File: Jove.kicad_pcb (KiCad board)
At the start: 2 copper layers, 65 x 100 mm, 153 parts, among them J1 PJ301B, J2 PJ301B, J3 PJ301B, J4 PJ301B, J5 PJ301B, J6 PJ301B, P1 CONN_02X05, Q1 BCM857BS, Q2 BCM857BS, Q3 J112, Q4 J112, Q5 J112, Q6 J112, SW1 KS-01Q, U1 TL072-, U10 CD4027, U11 CD40106, U12 TS321, U13 TS321, U2 TL072-, U3 TL072-, U4 TL072-, U5 LM13700, U6 LM13700, U7 LM13700, U8 DG409, U9 CD4052

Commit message: commit before making panel branch
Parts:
- added REF**: fiducial-1mm, MyModules:fiducial-1mm, B.Cu at (15.0, 15.0)
- added REF**: fiducial-1mm, MyModules:fiducial-1mm, B.Cu at (74.5, 109.5)
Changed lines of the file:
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@@
     (thickness 1.6)
     (drawings 45)
-    (tracks 1170)
+    (tracks 1171)
     (zones 0)
-    (modules 153)
+    (modules 155)
     (nets 114)
   )
@@
     (pad_to_mask_clearance 0)
     (aux_axis_origin 0 0)
-    (visible_elements 7FFFB7FF)
+    (visible_elements 7FFFF77F)
     (pcbplotparams
       (layerselection 0x010f0_80000001)
@@
     (add_net -12V)
   )
+  (module MyModules:SM0603-R-JRL (layer B.Cu)
+    (at 17.8 21.75 270)
+    (attr smd)
+    (fp_text reference R76 (at 2 -0.1 360) (layer B.SilkS)
+      (effects (font (size 0.6096 0.6096) (thickness 0.1524)) (justify mirror))
+    )
+    (fp_text value 100K (at 0 0 270) (layer B.SilkS) hide
+      (effects (font (size 0.508 0.4572) (thickness 0.1143)) (justify mirror))
+    )
+    (fp_line (start -1.4 0.8) (end -0.5 0.8) (layer B.SilkS) (width 0.2))
+    (fp_line (start 1.4 -0.8) (end 1.4 0.8) (layer B.SilkS) (width 0.2))
+    (fp_line (start -1.4 0.8) (end -1.4 -0.8) (layer B.SilkS) (width 0.2))
+    (fp_line (start -1.4 -0.8) (end -0.5 -0.8) (layer B.SilkS) (width 0.2))
+    (fp_line (start 0.5 0.8) (end 1.4 0.8) (layer B.SilkS) (width 0.2))
+    (fp_line (start 0.5 -0.8) (end 1.4 -0.8) (layer B.SilkS) (width 0.2))
+    (pad 1 smd rect (at -0.8509 0 270) (size 0.8128 1.143) (layers B.Cu B.Paste B.Mask)
+      (net 85 "Net-(R76-Pad1)"))
+    (pad 2 smd rect (at 0.8509 0 270) (size 0.8128 1.143) (layers B.Cu B.Paste B.Mask)
+      (net 32 "Net-(J2-Pad3)"))
+    (model Resistors_SMD.3dshapes/R_0603.wrl
+      (at (xyz 0 0 0.001))
+      (scale (xyz 1 1 1))
+      (rotate (xyz 0 0 0))
+    )
+  )
   (module "SMD TRAN:sot323-6" (layer B.Cu)
     (at 37.75 26 270)
@@
   )
   (module MyModules:SM0603-R-JRL (layer B.Cu)
-    (at 17.8 21.75 270)
-    (attr smd)
-    (fp_text reference R76 (at 2 -0.1 360) (layer B.SilkS)
-      (effects (font (size 0.6096 0.6096) (thickness 0.1524)) (justify mirror))
-    )
-    (fp_text value 100K (at 0 0 270) (layer B.SilkS) hide
-      (effects (font (size 0.508 0.4572) (thickness 0.1143)) (justify mirror))
-    )
-    (fp_line (start -1.4 0.8) (end -0.5 0.8) (layer B.SilkS) (width 0.2))
-    (fp_line (start 1.4 -0.8) (end 1.4 0.8) (layer B.SilkS) (width 0.2))
-    (fp_line (start -1.4 0.8) (end -1.4 -0.8) (layer B.SilkS) (width 0.2))
-    (fp_line (start -1.4 -0.8) (end -0.5 -0.8) (layer B.SilkS) (width 0.2))
-    (fp_line (start 0.5 0.8) (end 1.4 0.8) (layer B.SilkS) (width 0.2))
-    (fp_line (start 0.5 -0.8) (end 1.4 -0.8) (layer B.SilkS) (width 0.2))
-    (pad 1 smd rect (at -0.8509 0 270) (size 0.8128 1.143) (layers B.Cu B.Paste B.Mask)
-      (net 85 "Net-(R76-Pad1)"))
-    (pad 2 smd rect (at 0.8509 0 270) (size 0.8128 1.143) (layers B.Cu B.Paste B.Mask)
-      (net 32 "Net-(J2-Pad3)"))
-    (model Resistors_SMD.3dshapes/R_0603.wrl
-      (at (xyz 0 0 0.001))
-      (scale (xyz 1 1 1))
-      (rotate (xyz 0 0 0))
-    )
-  )
-  (module MyModules:SM0603-R-JRL (layer B.Cu)
     (at 21 21.75 270)
     (attr smd)
@@
     )
   )
+  (module MyModules:fiducial-1mm (layer B.Cu)
+    (at 15 15)
+    (fp_text reference REF** (at 0 -0.5) (layer B.SilkS) hide
+      (effects (font (size 1 1) (thickness 0.15)) (justify mirror))
+    )
+    (fp_text value fiducial-1mm (at 0 0.5) (layer B.Fab) hide
+      (effects (font (size 1 1) (thickness 0.15)) (justify mirror))
+    )
+    (pad 1 smd oval (at 0 0) (size 1 1) (layers B.Cu B.Paste B.Mask)
+      (solder_mask_margin 0.5) (clearance 0.75))
+  )
+  (module MyModules:fiducial-1mm (layer B.Cu)
+    (at 74.5 109.5)
+    (fp_text reference REF** (at 0 -0.5) (layer B.SilkS) hide
+      (effects (font (size 1 1) (thickness 0.15)) (justify mirror))
+    )
+    (fp_text value fiducial-1mm (at 0 0.5) (layer B.Fab) hide
+      (effects (font (size 1 1) (thickness 0.15)) (justify mirror))
+    )
+    (pad 1 smd oval (at 0 0) (size 1 1) (layers B.Cu B.Paste B.Mask)
+      (solder_mask_margin 0.5) (clearance 0.75))
+  )
   (gr_text MODE (at 54.75 15) (layer F.SilkS)
     (effects (font (size 1.5 1.5) (thickness 0.3)))
@@
   (segment (start 13.3 62.688466) (end 13.3 81.9) (width 0.254) (layer B.Cu) (net 32) (status 10))
   (segment (start 13.3 81.9) (end 19 87.6) (width 0.254) (layer B.Cu) (net 32))
-  (segment (start 67.081463 84.681463) (end 67.081463 56.525685) (width 0.254) (layer B.Cu) (net 33))
-  (segment (start 70 87.6) (end 67.081463 84.681463) (width 0.254) (layer B.Cu) (net 33))
+  (segment (start 70 87.6) (end 70 66.5) (width 0.254) (layer B.Cu) (net 33))
+  (segment (start 70 66.5) (end 67.081463 63.581463) (width 0.254) (layer B.Cu) (net 33))
+  (segment (start 67.081463 63.581463) (end 67.081463 56.525685) (width 0.254) (layer B.Cu) (net 33))
   (segment (start 56 101.6) (end 56 99.6) (width 0.254) (layer F.Cu) (net 34))
   (segment (start 56 99.6) (end 60.7 94.9) (width 0.254) (layer F.Cu) (net 34))

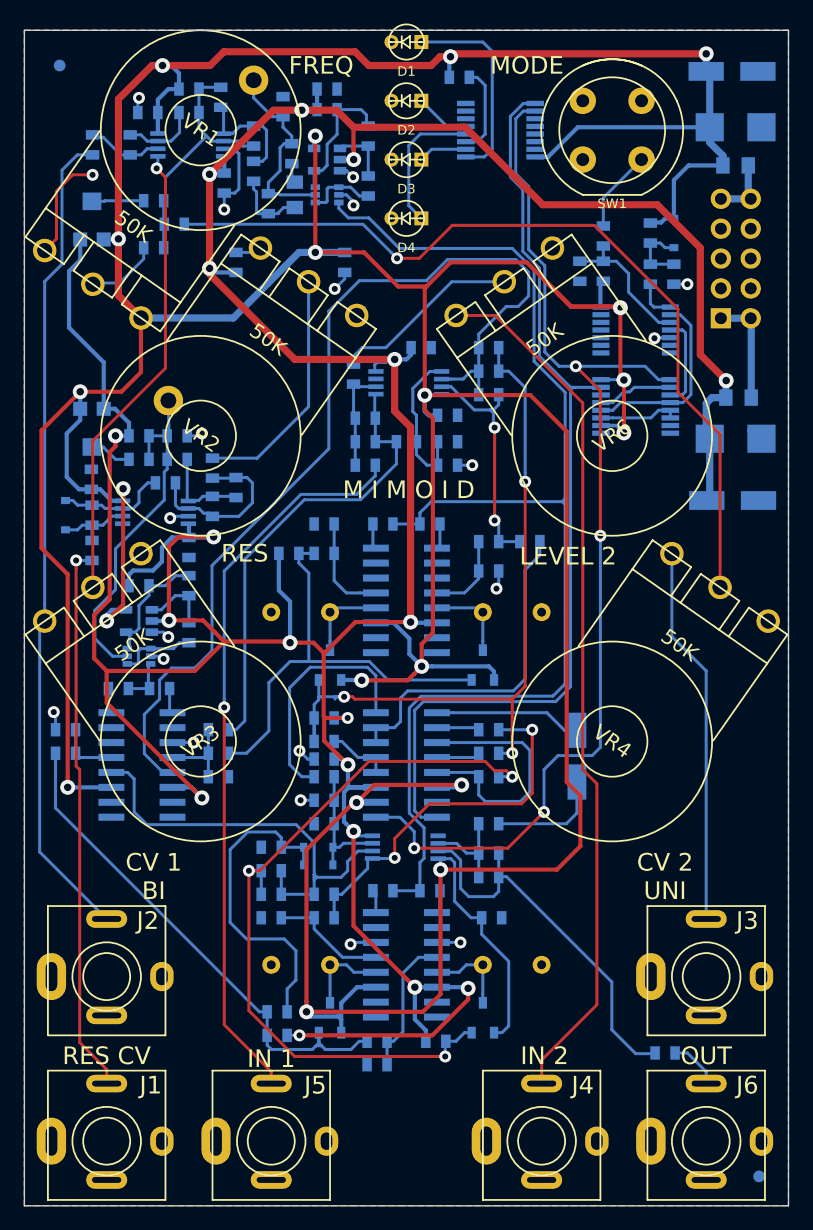
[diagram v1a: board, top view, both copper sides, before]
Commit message: updated 0603 footprints to square pads to please assembler, added logo, tweaked main rail traces
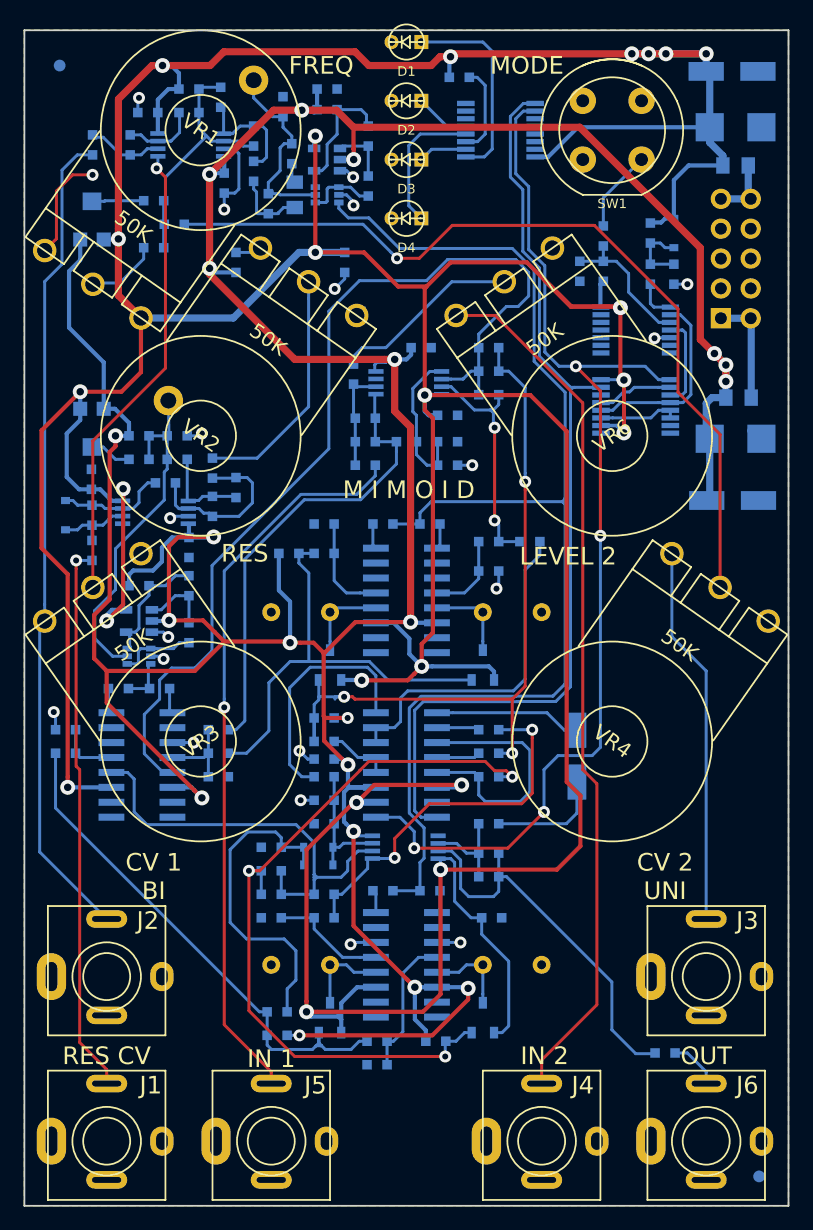
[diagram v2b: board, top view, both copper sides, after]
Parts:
- added REF***: OSHW-Symbol_6.7x6mm_SilkScreen, Symbols:OSHW-Symbol_6.7x6mm_SilkScreen, B.Cu at (44.5, 107.5)
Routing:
- net +12V: track 493.8 -> 500.1 mm, vias 20 -> 23
- net -12V: track 337.3 -> 340.1 mm, vias 18 -> 20

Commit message: genereated gerbers for panelization by PCB house
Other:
- board text added: "JOVE"
- board text added: "Multimode Filter v1.4 01 2017"
- board text removed: "Multimode Filter v1.3 10 2016"
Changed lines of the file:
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@@
     (area 11.924999 11.924999 77.075001 112.075001)
     (thickness 1.6)
-    (drawings 832)
+    (drawings 833)
     (tracks 1183)
     (zones 0)
@@
   )
   (setup
-    (last_trace_width 0.6096)
+    (last_trace_width 0.254)
     (user_trace_width 0.2032)
     (user_trace_width 0.254)
@@
       (xy 0.555814 2.531069)) (layer B.SilkS) (width 0.01))
   )
+  (gr_text JOVE (at 66.04 78.105) (layer B.SilkS)
+    (effects (font (size 1.5 1.5) (thickness 0.3)) (justify mirror))
+  )
   (gr_line (start 72.50984 81.776773) (end 72.432207 81.810639) (layer B.SilkS) (width 0.15))
   (gr_line (start 72.484971 83.523009) (end 72.519828 83.523662) (layer B.SilkS) (width 0.15))
@@
     (effects (font (size 1.5 1.5) (thickness 0.3)) (justify mirror))
   )
-  (gr_text "Multimode Filter\nv1.3 10 2016\n" (at 21.7 83.2) (layer B.SilkS)
+  (gr_text "Multimode Filter\nv1.4 01 2017\n" (at 21.7 83.2) (layer B.SilkS)
     (effects (font (size 1.5 1.5) (thickness 0.3)) (justify mirror))
   )

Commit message: changed R51 and R72 values to incrase overall output gain and bring down LP12 output levels to match other modes
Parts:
- R51: value 100K -> 330K
- R72: value 10K -> 270K
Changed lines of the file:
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@@
     (links 344)
     (no_connects 0)
-    (area 8.999999 -2.400001 80.067095 126.300001)
+    (area 11.924999 11.924999 77.075001 112.075001)
     (thickness 1.6)
     (drawings 833)
@@
       (effects (font (size 0.6096 0.6096) (thickness 0.1524)) (justify mirror))
     )
-    (fp_text value 100K (at 0 0 180) (layer B.SilkS) hide
+    (fp_text value 330K (at 0 0 180) (layer B.SilkS) hide
       (effects (font (size 0.508 0.4572) (thickness 0.1143)) (justify mirror))
     )
@@
       (effects (font (size 0.6096 0.6096) (thickness 0.1524)) (justify mirror))
     )
-    (fp_text value 10K (at 0 0) (layer B.SilkS) hide
+    (fp_text value 270K (at 0 0) (layer B.SilkS) hide
       (effects (font (size 0.508 0.4572) (thickness 0.1143)) (justify mirror))
     )

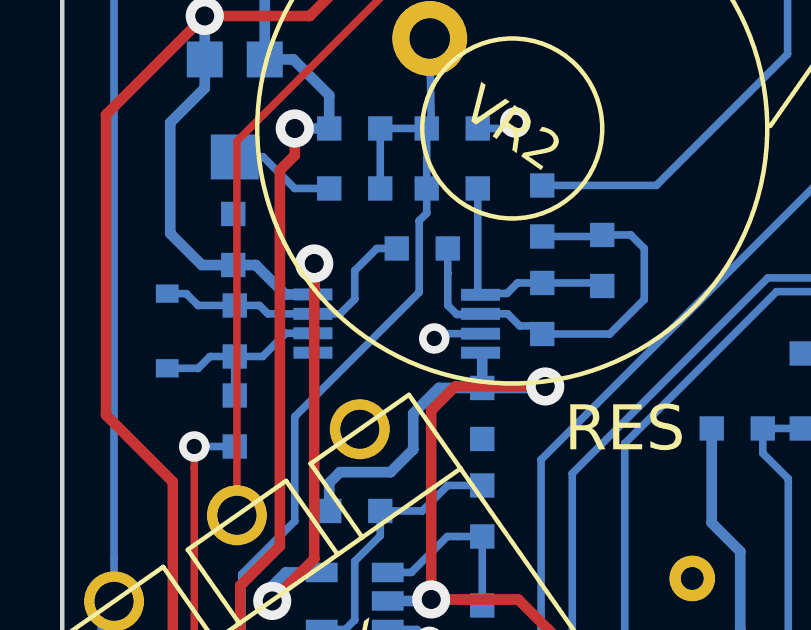
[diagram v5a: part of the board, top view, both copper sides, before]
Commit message: updated BOM, readme, added octopart link
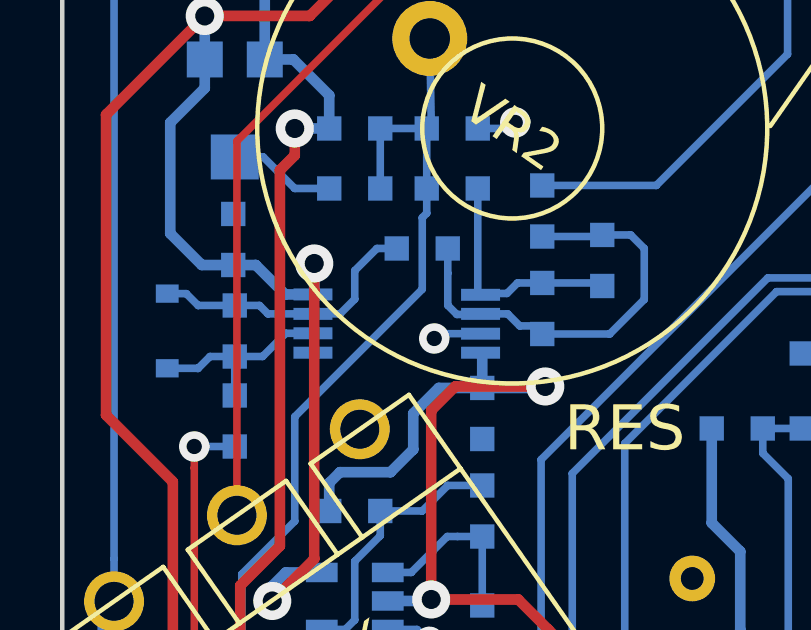
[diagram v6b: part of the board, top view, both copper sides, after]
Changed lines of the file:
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@@
     (links 344)
     (no_connects 0)
-    (area 11.924999 11.924999 77.075001 112.075001)
+    (area 8.999999 -2.400001 80.067095 126.300001)
     (thickness 1.6)
     (drawings 833)
@@
   (segment (start 22.54756 67.89846) (end 22.6491 68) (width 0.254) (layer B.Cu) (net 40))
   (segment (start 22.6491 68) (end 20.8509 68) (width 0.254) (layer B.Cu) (net 40))
-  (segment (start 17.983998 61.355684) (end 17.983998 63.733998) (width 0.254) (layer B.Cu) (net 41))
-  (segment (start 24.1491 49.3255) (end 23.897662 49.576938) (width 0.254) (layer B.Cu) (net 41))
-  (segment (start 23.897662 49.576938) (end 23.897662 51.961798) (width 0.254) (layer B.Cu) (net 41))
-  (segment (start 19.75 59.589682) (end 17.983998 61.355684) (width 0.254) (layer B.Cu) (net 41))
   (segment (start 24.1491 48.5) (end 24.1491 49.3255) (width 0.254) (layer B.Cu) (net 41))
-  (segment (start 23.897662 51.961798) (end 19.75 56.10946) (width 0.254) (layer B.Cu) (net 41))
-  (segment (start 17.983998 63.733998) (end 19.5 65.25) (width 0.254) (layer B.Cu) (net 41))
+  (segment (start 19.75 59.589682) (end 17.983998 61.355684) (width 0.254) (layer B.Cu) (net 41))
+  (segment (start 24.1491 49.3255) (end 24 49.4746) (width 0.254) (layer B.Cu) (net 41))
   (segment (start 19.75 56.10946) (end 19.75 59.589682) (width 0.254) (layer B.Cu) (net 41))
+  (segment (start 24 49.4746) (end 24 51.85946) (width 0.254) (layer B.Cu) (net 41))
+  (segment (start 24 51.85946) (end 19.75 56.10946) (width 0.254) (layer B.Cu) (net 41))
+  (segment (start 17.983998 61.355684) (end 17.983998 63.733998) (width 0.254) (layer B.Cu) (net 41))
+  (segment (start 17.983998 63.733998) (end 19.5 65.25) (width 0.254) (layer B.Cu) (net 41))
   (segment (start 19.5 65.25) (end 20.95244 65.25) (width 0.254) (layer B.Cu) (net 41))
   (segment (start 24.25 43.5) (end 24.3 46.3491) (width 0.254) (layer B.Cu) (net 41) (status 10))

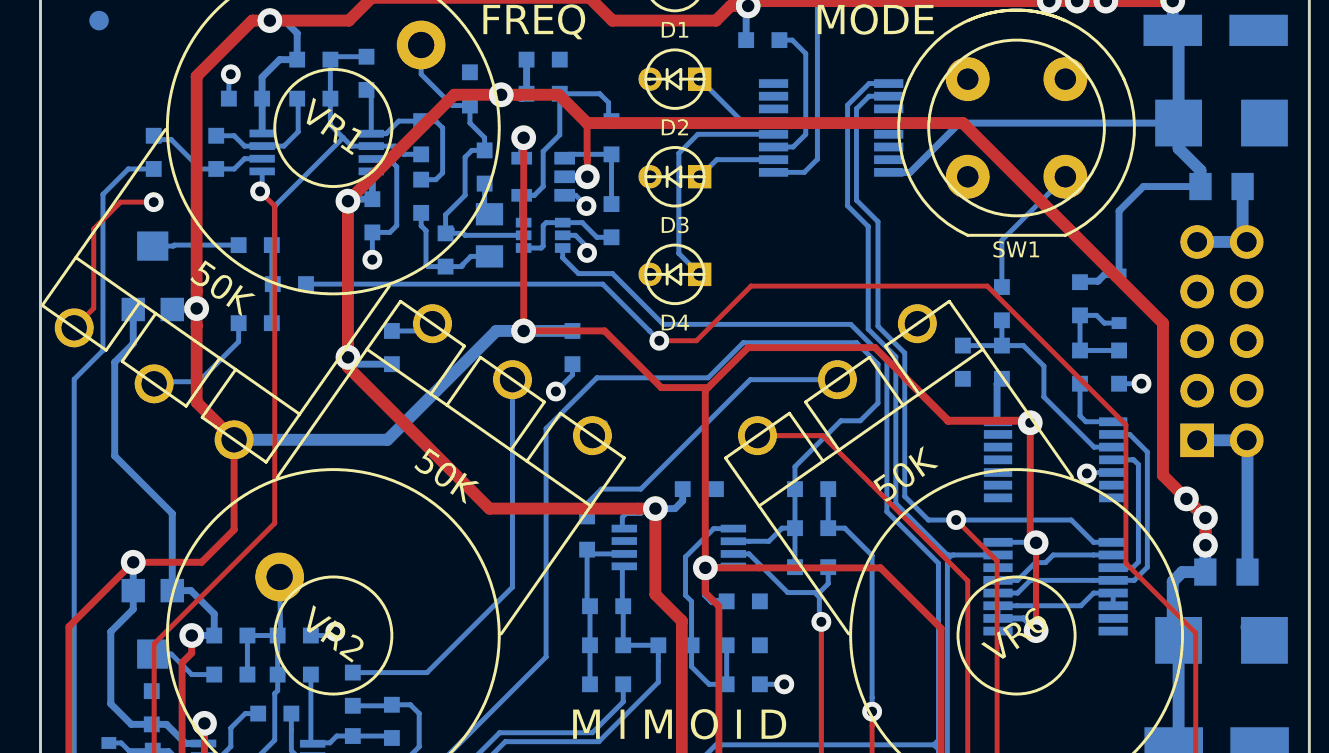
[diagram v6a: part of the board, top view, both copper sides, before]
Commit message: moved -12V trace away from SW1 and power header
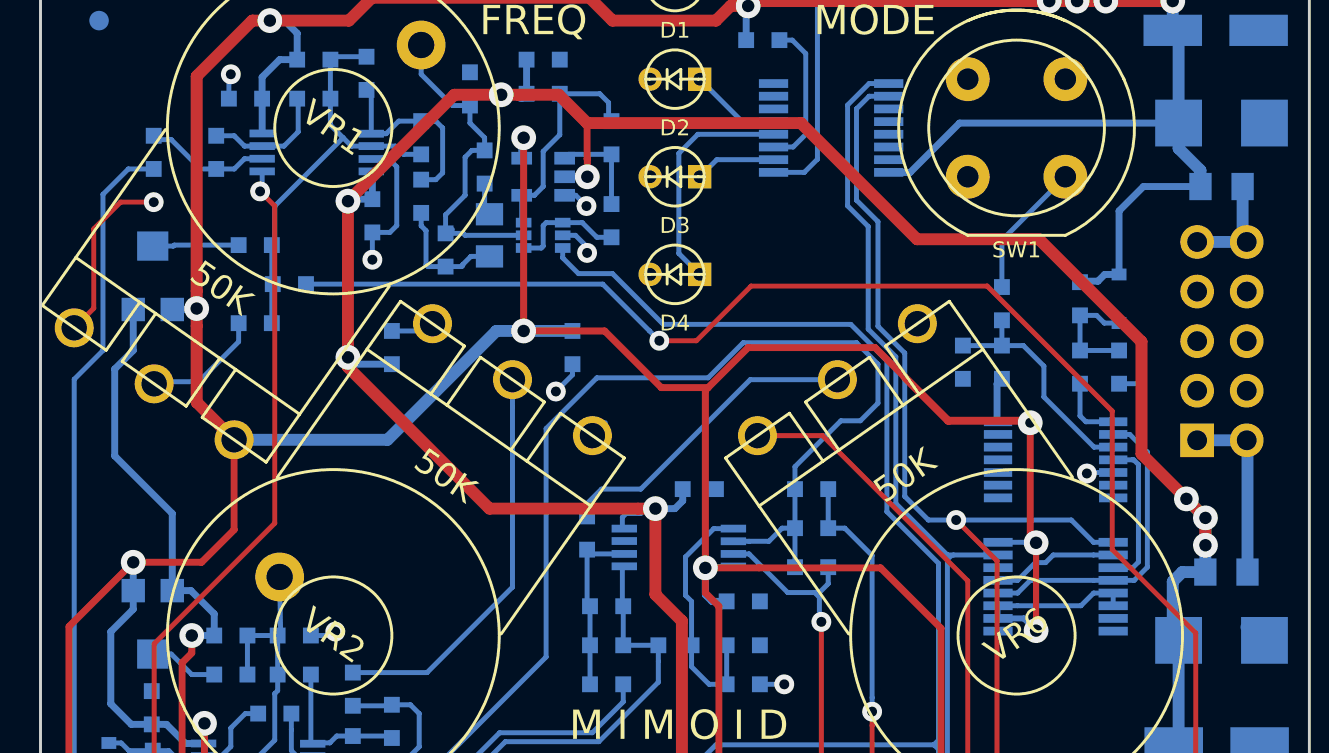
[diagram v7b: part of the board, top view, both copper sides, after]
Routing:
- net -12V: track 340.1 -> 338.9 mm
- net GND: vias 20 -> 19
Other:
- board text added: "Multimode Filter v1.5 11 2017"
- board text removed: "Multimode Filter v1.4 01 2017"

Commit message: first rohs commit
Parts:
- added G***: LOGO, LOGO, B.Cu at (66.8, 74.8)
- added G***: LOGO, LOGO, B.Cu at (73.2, 74.8)
- added G***: LOGO, w_logo:Logo_silk_WEEE_3.4x5mm, B.Cu at (57.5, 50.0)
- added G***: LOGO, Logos:80_logo_7.5mm, B.Cu at (44.5, 33.2)
- added G***: LOGO, w_logo:Logo_silk_ROHS_5x2.8mm, B.Cu at (66.2, 50.0)
- added G***: LOGO, w_logo:Logo_silk_Lead-Free_5x5mm, B.Cu at (62.0, 50.0)
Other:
- rule pad_to_mask_clearance: 0 -> 0.05
- board text added: "MULITMODE FILTER v1.5 11 2017"
- board text removed: "JOVE"
- board text removed: "Multimode Filter v1.5 11 2017"
